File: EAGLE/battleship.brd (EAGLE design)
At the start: 120 x 90 mm, 27 parts, among them IC1 EK-TM4C123GXLP

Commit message: edit boards
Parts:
- added SJ3, SJ4: (no value), jumper:SJ
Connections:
- net BL: now also SJ3.2, SJ4.1
- net GND: now also SJ3.1
- net LIGHT: now also SJ4.2
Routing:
- net BL: track 106.0 -> 115.9 mm
- net LIGHT: track 8.62 -> 14.5 mm
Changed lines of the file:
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@@
 <drawing>
 <settings>
-<setting alwaysvectorfont="yes"/>
+<setting alwaysvectorfont="no"/>
 <setting verticaltext="up"/>
 </settings>
@@
 <attribute name="SPICEPREFIX" value="R" x="19.05" y="10.16" size="1.778" layer="27" rot="R90" display="off"/>
 </element>
+<element name="SJ3" library="jumper" library_urn="urn:adsk.eagle:library:252" package="SJ" package3d_urn="urn:adsk.eagle:package:15471/1" value="" x="17.78" y="19.05">
+<attribute name="VALUE" x="18.1801" y="19.05" size="0.02" layer="27"/>
+</element>
+<element name="SJ4" library="jumper" library_urn="urn:adsk.eagle:library:252" package="SJ" package3d_urn="urn:adsk.eagle:package:15471/1" value="" x="15.24" y="10.16" rot="R270">
+<attribute name="VALUE" x="15.24" y="9.7599" size="0.02" layer="27" rot="R270"/>
+</element>
 </elements>
 <signals>
@@
 <via x="111.76" y="49.53" extent="1-16" drill="0.4064"/>
 <via x="7.62" y="69.85" extent="1-16" drill="0.4064"/>
+<contactref element="SJ3" pad="1"/>
 </signal>
 <signal name="N$21">
@@
 <wire x1="20.5" y1="6.5" x2="20.5" y2="8.562" width="1.143" layer="1"/>
 <wire x1="20.5" y1="8.562" x2="22.098" y2="10.16" width="1.143" layer="1"/>
+<contactref element="SJ4" pad="2"/>
+<wire x1="15.24" y1="9.398" x2="19.05" y2="5.588" width="1.143" layer="1"/>
+<wire x1="19.05" y1="5.588" x2="19.05" y2="5.08" width="1.143" layer="1"/>
 </signal>
 <signal name="RX">
@@
 <contactref element="JP5" pad="4"/>
 <contactref element="JP5" pad="3"/>
-<wire x1="29.21" y1="6.35" x2="31.75" y2="6.35" width="0.4064" layer="1"/>
-<wire x1="31.75" y1="6.35" x2="37.14" y2="6.35" width="0.4064" layer="1"/>
 <contactref element="SJ2" pad="1"/>
-<wire x1="29.21" y1="6.35" x2="23.622" y2="6.35" width="0.4064" layer="1"/>
+<wire x1="23.622" y1="6.35" x2="29.21" y2="6.35" width="1.143" layer="1"/>
+<wire x1="29.21" y1="6.35" x2="31.75" y2="6.35" width="1.143" layer="1"/>
+<wire x1="31.75" y1="6.35" x2="37.14" y2="6.35" width="1.143" layer="1"/>
 </signal>
 <signal name="N$36">
@@
 <wire x1="22.5" y1="27.5" x2="22.5" y2="18.69" width="1.143" layer="1"/>
 <wire x1="22.5" y1="18.69" x2="19.05" y2="15.24" width="1.143" layer="1"/>
+<contactref element="SJ3" pad="2"/>
+<contactref element="SJ4" pad="1"/>
+<wire x1="15.24" y1="10.922" x2="19.05" y2="14.732" width="1.143" layer="1"/>
+<wire x1="19.05" y1="14.732" x2="19.05" y2="15.24" width="1.143" layer="1"/>
+<wire x1="18.542" y1="19.05" x2="19.05" y2="18.542" width="1.143" layer="1"/>
+<wire x1="19.05" y1="18.542" x2="19.05" y2="15.24" width="1.143" layer="1"/>
 </signal>
 </signals>

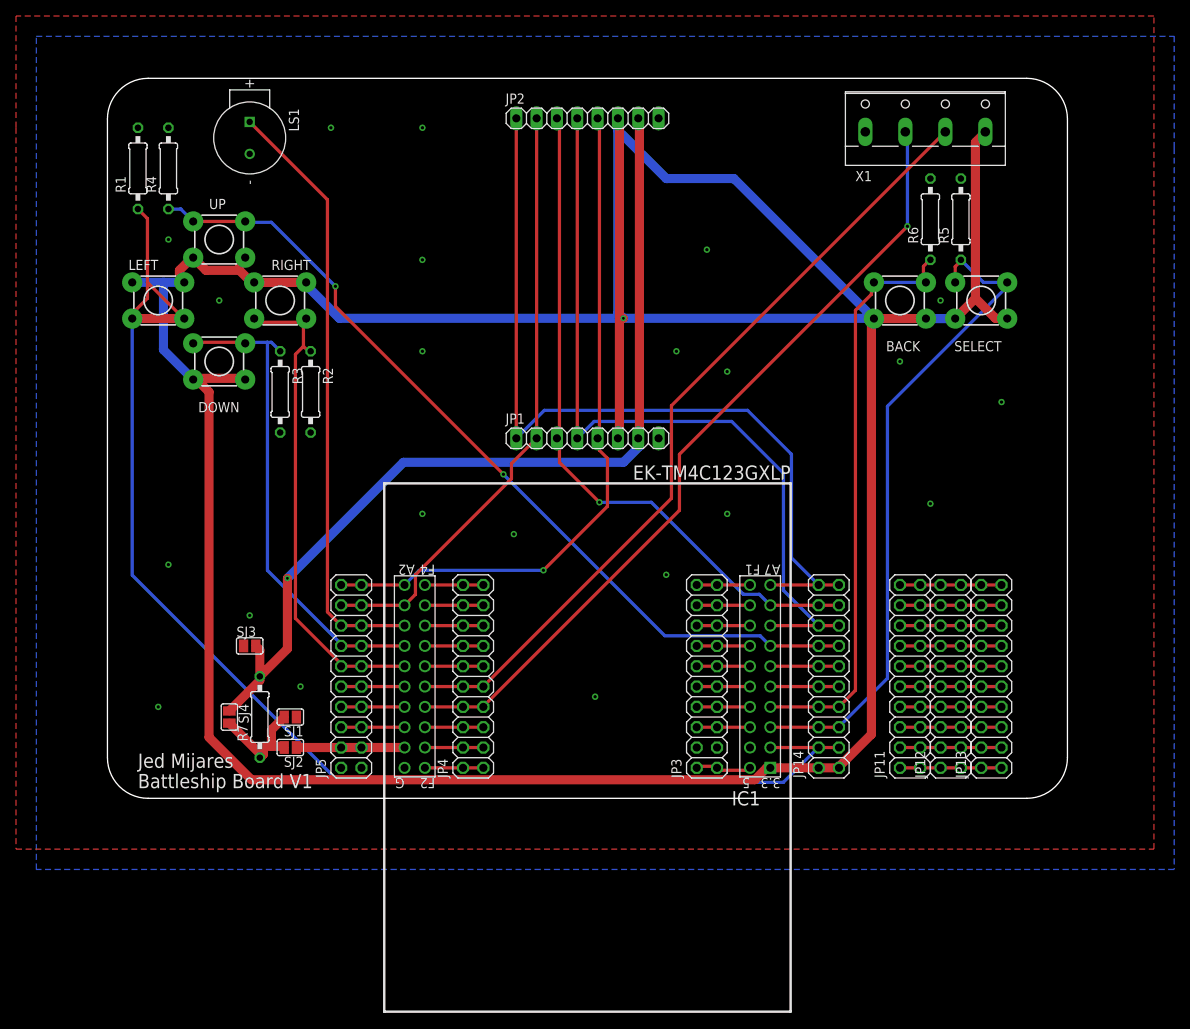
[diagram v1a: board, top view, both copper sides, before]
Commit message: reduced PCB size
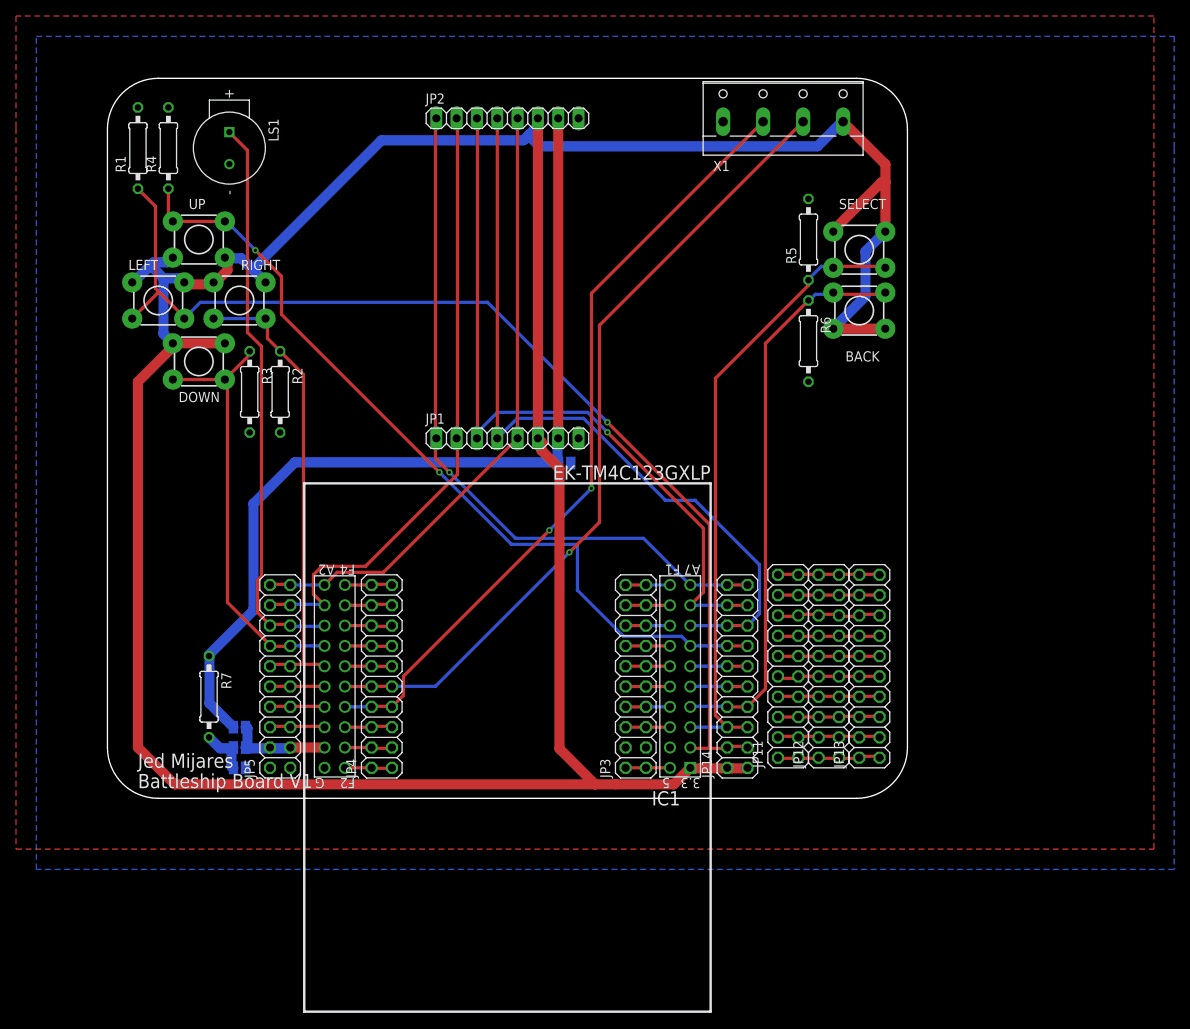
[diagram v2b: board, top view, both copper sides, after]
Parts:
- moved SJ1 46.7 mm to (57.1, 41.9), flipped to the bottom
- moved R6 21.6 mm to (87.6, 57.1), turned to 270 degrees
- moved R5 19.2 mm to (87.6, 69.8)
- moved X1 17.8 mm to (84.5, 85.9)
- moved SELECT 16.5 mm to (94.0, 68.6), turned to 180 degrees
- moved SJ3 15.3 mm to (16.5, 3.81), flipped to the bottom, turned to 180 degrees
- moved JP11 15.3 mm to (85.1, 16.5)
- moved JP12 15.3 mm to (90.2, 16.5)
- moved JP13 15.3 mm to (95.2, 16.5)
- moved JP14 11.4 mm to (78.7, 15.2)
- moved JP4 11.4 mm to (34.3, 15.2)
- moved IC1 10.0 mm to (50.0, 16.5)
- moved JP1 10.0 mm to (50.0, 45.0)
- moved JP2 10.0 mm to (50.0, 85.0)
- moved JP3 8.89 mm to (66.0, 15.2)
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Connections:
- removed net LIGHT: R7.1, SJ1.2, SJ2.2, SJ4.2
- removed net N$34: IC1.19, JP5.3, JP5.4, SJ2.1
- new net BLPIN: IC1.19, JP5.3, JP5.4, SJ2.1, SJ4.2
- new net N$6: R7.2, SJ3.1, SJ4.1
- net BL: now also R7.1, SJ1.1, SJ2.2; no longer R7.2, SJ3.2, SJ4.1
- net GND: now also SJ1.2, SJ3.2; no longer SJ1.1, SJ3.1
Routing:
- net 3.3V: track 455.9 -> 390.1 mm, vias 1 -> 0
- net LEFTSIG: track 167.1 -> 136.9 mm, vias 0 -> 1
- net RESET: track 104.4 -> 88.3 mm, vias 0 -> 1
- net LIGHT: track 14.5 -> 0.00 mm
- net N$34: track 13.5 -> 0.00 mm
- net BLPIN: track 0.00 -> 12.7 mm
- net CLK: track 86.6 -> 78.6 mm, vias 1 -> 0
- net DC: track 85.8 -> 93.7 mm
- net DOWNSIG: track 61.1 -> 53.8 mm
- net N$6: track 0.00 -> 6.20 mm
- net BUZZERPIN: track 75.6 -> 71.2 mm
- net SELECTSIG: track 83.0 -> 79.1 mm
- net CE: track 75.6 -> 79.4 mm
- net UPSIG: track 107.9 -> 104.3 mm
- net RX: track 101.3 -> 98.3 mm, vias 1 -> 2
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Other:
- board size 120 x 90 mm -> 100 x 90 mm

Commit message: update board and dxf
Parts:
- added JP6: (no value), pinhead:2X10
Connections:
- new net N$1: JP6.1, JP6.2
- new net N$10: JP6.19, JP6.20
- new net N$11: JP6.17, JP6.18
- new net N$2: JP6.3, JP6.4
- new net N$3: JP6.5, JP6.6
- new net N$4: JP6.7, JP6.8
- new net N$5: JP6.10, JP6.9
- new net N$7: JP6.11, JP6.12
- new net N$8: JP6.13, JP6.14
- new net N$9: JP6.15, JP6.16
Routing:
- net N$9: track 0.00 -> 2.54 mm
- net N$8: track 0.00 -> 2.54 mm
- net N$7: track 0.00 -> 2.54 mm
- net N$5: track 0.00 -> 2.54 mm
- net N$4: track 0.00 -> 2.54 mm
- net N$3: track 0.00 -> 2.54 mm
- net N$2: track 0.00 -> 2.54 mm
- net N$11: track 0.00 -> 2.54 mm
- net N$10: track 0.00 -> 2.54 mm
- net N$1: track 0.00 -> 2.54 mm
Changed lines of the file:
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@@
 <wire x1="6.35" y1="0" x2="93.65" y2="0" width="0" layer="20"/>
 <wire x1="93.65" y1="0" x2="100" y2="6.35" width="0" layer="20" curve="90"/>
-<text x="3.81" y="3.81" size="1.778" layer="21">Jed Mijares</text>
-<text x="3.81" y="1.27" size="1.778" layer="21">Battleship Board V1</text>
+<text x="96.52" y="31.75" size="1.778" layer="21" rot="R90">Jed Mijares</text>
+<text x="99.06" y="31.75" size="1.778" layer="21" rot="R90">Battleship Board V1</text>
 </plain>
 <attributes>
@@
 <attribute name="SPICEPREFIX" value="R" x="12.7" y="12.7" size="1.778" layer="27" rot="R270" display="off"/>
 </element>
+<element name="JP6" library="pinhead" library_urn="urn:adsk.eagle:library:325" package="2X10" package3d_urn="urn:adsk.eagle:package:22405/2" value="" x="10.16" y="34.29" rot="MR90">
+<attribute name="VALUE" x="5.715" y="21.59" size="1.27" layer="28" rot="MR90"/>
+</element>
 </elements>
 <signals>
@@
 <wire x1="71.75" y1="20.25" x2="72.75" y2="19.25" width="0.4064" layer="16"/>
 <wire x1="64.5" y1="20.25" x2="71.75" y2="20.25" width="0.4064" layer="16"/>
-<wire x1="58.75" y1="26" x2="64.5" y2="20.25" width="0.4064" layer="16"/>
-<wire x1="58.75" y1="31.75" x2="58.75" y2="26" width="0.4064" layer="16"/>
-<wire x1="50.5" y1="31.75" x2="58.75" y2="31.75" width="0.4064" layer="16"/>
+<wire x1="64.5" y1="20.25" x2="61.425" y2="23.325" width="0.4064" layer="16"/>
+<wire x1="58.75" y1="31.75" x2="50.5" y2="31.75" width="0.4064" layer="16"/>
 <wire x1="41.5" y1="40.75" x2="50.5" y2="31.75" width="0.4064" layer="16"/>
 <wire x1="21.75" y1="60.5" x2="41.5" y2="40.75" width="0.4064" layer="1"/>
@@
 <wire x1="77.47" y1="19.05" x2="72.86" y2="19.05" width="0.4064" layer="16"/>
 <wire x1="77.47" y1="19.05" x2="80.01" y2="19.05" width="0.4064" layer="1"/>
+<wire x1="61.425" y1="23.325" x2="61.425" y2="29.075" width="0.4064" layer="16"/>
+<wire x1="61.425" y1="29.075" x2="58.75" y2="31.75" width="0.4064" layer="16"/>
 </signal>
 <signal name="SELECTSIG">
@@
 <wire x1="35.5" y1="14" x2="35.56" y2="13.97" width="0.4064" layer="1"/>
 <wire x1="33.25" y1="14" x2="33.02" y2="13.97" width="0.4064" layer="1"/>
-<wire x1="57.75" y1="30.75" x2="61.5" y2="34.5" width="0.4064" layer="1"/>
+<wire x1="57.75" y1="30.75" x2="58.585" y2="31.585" width="0.4064" layer="1"/>
+<wire x1="58.585" y1="31.585" x2="61.5" y2="34.5" width="0.4064" layer="1"/>
 <wire x1="41" y1="14" x2="57.75" y2="30.75" width="0.4064" layer="16"/>
 <via x="57.75" y="30.75" extent="1-16" drill="0.4064"/>
@@
 <wire x1="14.07" y1="6.25" x2="15.5" y2="6.25" width="1.27" layer="16"/>
 </signal>
+<signal name="N$1">
+<contactref element="JP6" pad="1"/>
+<contactref element="JP6" pad="2"/>
+<wire x1="8.89" y1="22.86" x2="11.43" y2="22.86" width="0.4064" layer="16"/>
+</signal>
+<signal name="N$2">
+<contactref element="JP6" pad="4"/>
+<contactref element="JP6" pad="3"/>
+<wire x1="8.89" y1="25.4" x2="11.43" y2="25.4" width="0.4064" layer="16"/>
+</signal>
+<signal name="N$3">
+<contactref element="JP6" pad="5"/>
+<contactref element="JP6" pad="6"/>
+<wire x1="8.89" y1="27.94" x2="11.43" y2="27.94" width="0.4064" layer="16"/>
+</signal>
+<signal name="N$4">
+<contactref element="JP6" pad="8"/>
+<contactref element="JP6" pad="7"/>
+<wire x1="8.89" y1="30.48" x2="11.43" y2="30.48" width="0.4064" layer="16"/>
+</signal>
+<signal name="N$5">
+<contactref element="JP6" pad="9"/>
+<contactref element="JP6" pad="10"/>
+<wire x1="8.89" y1="33.02" x2="11.43" y2="33.02" width="0.4064" layer="16"/>
+</signal>
+<signal name="N$7">
+<contactref element="JP6" pad="12"/>
+<contactref element="JP6" pad="11"/>
+<wire x1="8.89" y1="35.56" x2="11.43" y2="35.56" width="0.4064" layer="16"/>
+</signal>
+<signal name="N$8">
+<contactref element="JP6" pad="13"/>
+<contactref element="JP6" pad="14"/>
+<wire x1="8.89" y1="38.1" x2="11.43" y2="38.1" width="0.4064" layer="16"/>
+</signal>
+<signal name="N$9">
+<contactref element="JP6" pad="16"/>
+<contactref element="JP6" pad="15"/>
+<wire x1="8.89" y1="40.64" x2="11.43" y2="40.64" width="0.4064" layer="16"/>
+</signal>
+<signal name="N$10">
+<contactref element="JP6" pad="19"/>
+<contactref element="JP6" pad="20"/>
+<wire x1="8.89" y1="45.72" x2="11.43" y2="45.72" width="0.4064" layer="16"/>
+</signal>
+<signal name="N$11">
+<contactref element="JP6" pad="18"/>
+<contactref element="JP6" pad="17"/>
+<wire x1="8.89" y1="43.18" x2="11.43" y2="43.18" width="0.4064" layer="16"/>
+</signal>
 </signals>

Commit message: minor board updates
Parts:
- renumbered JP1 to DISPLAY, JP2 to DISPLAY2
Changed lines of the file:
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@@
 <drawing>
 <settings>
-<setting alwaysvectorfont="yes"/>
+<setting alwaysvectorfont="no"/>
 <setting verticaltext="up"/>
 </settings>
@@
 <attribute name="PRICE" value="None" x="15.24" y="81.28" size="1.778" layer="27" rot="R270" display="off"/>
 </element>
-<element name="JP1" library="pinhead" library_urn="urn:adsk.eagle:library:325" package="1X08" package3d_urn="urn:adsk.eagle:package:22409/2" value="Display" x="50" y="45"/>
-<element name="JP2" library="pinhead" library_urn="urn:adsk.eagle:library:325" package="1X08" package3d_urn="urn:adsk.eagle:package:22409/2" value="Display" x="50" y="85">
+<element name="DISPLAY" library="pinhead" library_urn="urn:adsk.eagle:library:325" package="1X08" package3d_urn="urn:adsk.eagle:package:22409/2" value="Display" x="50" y="45"/>
+<element name="DISPLAY2" library="pinhead" library_urn="urn:adsk.eagle:library:325" package="1X08" package3d_urn="urn:adsk.eagle:package:22409/2" value="Display" x="50" y="85">
 <attribute name="VALUE" x="39.84" y="86.905" size="1.27" layer="27"/>
 </element>
@@
 <contactref element="LS1" pad="M"/>
 <polygon width="0.1524" layer="1">
-<vertex x="-11.43" y="83.82"/>
+<vertex x="-11.43" y="97.79"/>
 <vertex x="-11.43" y="-6.35"/>
-<vertex x="130.81" y="-6.35"/>
-<vertex x="130.81" y="97.79"/>
-<vertex x="-11.43" y="97.79"/>
+<vertex x="104.14" y="-6.35"/>
+<vertex x="104.14" y="97.79"/>
 </polygon>
 <polygon width="0.1524" layer="16">
-<vertex x="133.35" y="81.28"/>
-<vertex x="133.35" y="-8.89"/>
+<vertex x="107.95" y="95.25"/>
+<vertex x="107.95" y="-8.89"/>
 <vertex x="-8.89" y="-8.89"/>
 <vertex x="-8.89" y="95.25"/>
-<vertex x="133.35" y="95.25"/>
 </polygon>
-<contactref element="JP2" pad="8"/>
-<contactref element="JP1" pad="8"/>
+<contactref element="DISPLAY2" pad="8"/>
+<contactref element="DISPLAY" pad="8"/>
 <contactref element="X1" pad="1"/>
 <contactref element="JP3" pad="4"/>
@@
 </signal>
 <signal name="RESET">
-<contactref element="JP1" pad="1"/>
-<contactref element="JP2" pad="1"/>
+<contactref element="DISPLAY" pad="1"/>
+<contactref element="DISPLAY2" pad="1"/>
 <contactref element="IC1" pad="10"/>
 <contactref element="JP14" pad="20"/>
@@
 </signal>
 <signal name="CE">
-<contactref element="JP2" pad="2"/>
-<contactref element="JP1" pad="2"/>
+<contactref element="DISPLAY2" pad="2"/>
+<contactref element="DISPLAY" pad="2"/>
 <contactref element="IC1" pad="12"/>
 <contactref element="JP5" pad="17"/>
@@
 </signal>
 <signal name="DC">
-<contactref element="JP1" pad="3"/>
-<contactref element="JP2" pad="3"/>
+<contactref element="DISPLAY" pad="3"/>
+<contactref element="DISPLAY2" pad="3"/>
 <contactref element="IC1" pad="9"/>
 <contactref element="JP14" pad="17"/>
@@
 </signal>
 <signal name="DIN">
-<contactref element="JP2" pad="4"/>
-<contactref element="JP1" pad="4"/>
+<contactref element="DISPLAY2" pad="4"/>
+<contactref element="DISPLAY" pad="4"/>
 <contactref element="IC1" pad="8"/>
 <contactref element="JP14" pad="16"/>
@@
 </signal>
 <signal name="CLK">
-<contactref element="JP1" pad="5"/>
-<contactref element="JP2" pad="5"/>
+<contactref element="DISPLAY" pad="5"/>
+<contactref element="DISPLAY2" pad="5"/>
 <contactref element="IC1" pad="11"/>
 <contactref element="JP5" pad="20"/>
@@
 </signal>
 <signal name="3.3V" class="1">
-<contactref element="JP2" pad="6"/>
-<contactref element="JP1" pad="6"/>
+<contactref element="DISPLAY2" pad="6"/>
+<contactref element="DISPLAY" pad="6"/>
 <contactref element="X1" pad="4"/>
 <contactref element="UP" pad="4"/>
@@
 </signal>
 <signal name="BL" class="1">
-<contactref element="JP1" pad="7"/>
-<contactref element="JP2" pad="7"/>
+<contactref element="DISPLAY" pad="7"/>
+<contactref element="DISPLAY2" pad="7"/>
 <contactref element="SJ1" pad="1"/>
 <contactref element="SJ2" pad="2"/>
